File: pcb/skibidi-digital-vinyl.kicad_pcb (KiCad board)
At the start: 2 copper layers, 100 x 100 mm, 6 parts, among them U1 CH32V003FxUx, U2 BY25Q32ESHIG(R)

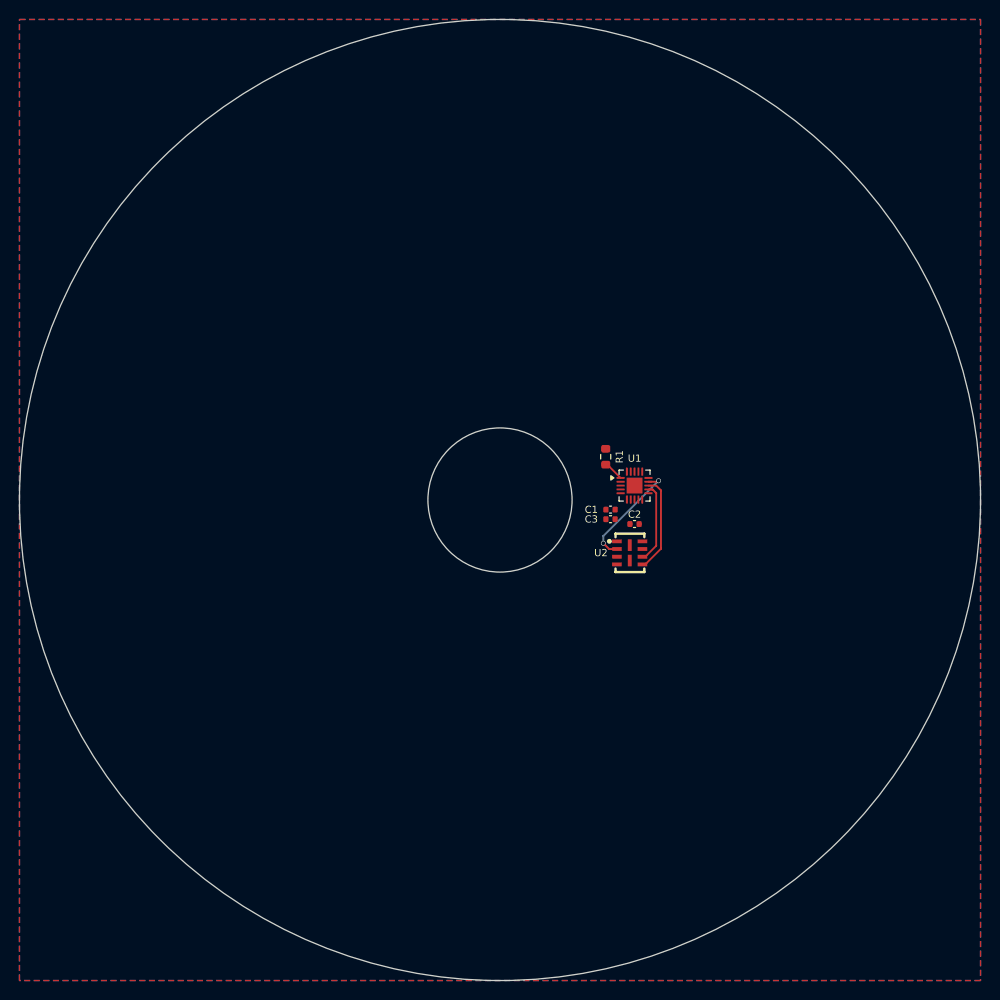
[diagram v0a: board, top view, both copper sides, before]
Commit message: disc routing done
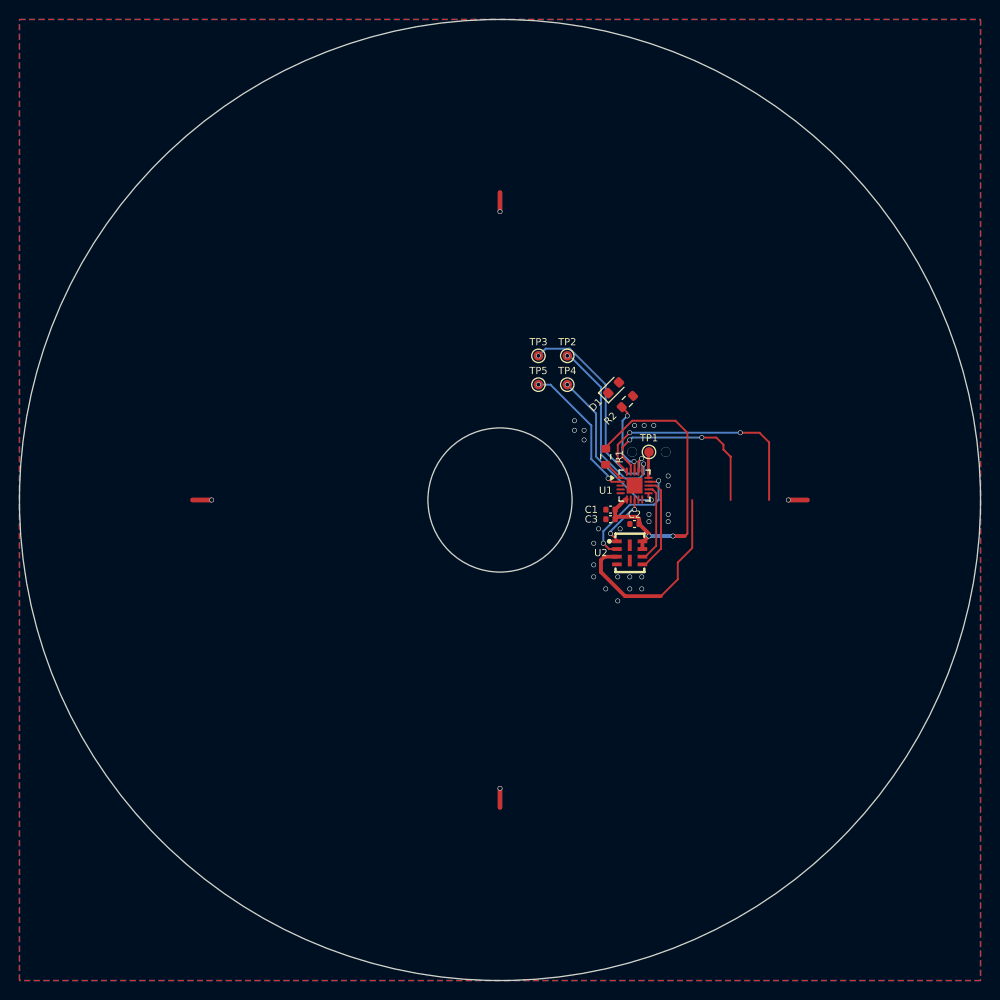
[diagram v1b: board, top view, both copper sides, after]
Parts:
- added D1: LED, LED_SMD:LED_0603_1608Metric, F.Cu at (161.8, 88.3)
- added R2: 1k, Resistor_SMD:R_0603_1608Metric, F.Cu at (163.2, 89.8)
- added TP1: TestPoint, TestPoint:TestPoint_Pad_D1.0mm, F.Cu at (165.5, 95.0)
- added TP2: TestPoint, TestPoint:TestPoint_Pad_D1.0mm, F.Cu at (157.0, 85.0)
- added TP3: TestPoint, TestPoint:TestPoint_Pad_D1.0mm, F.Cu at (154.0, 85.0)
- added TP4: TestPoint, TestPoint:TestPoint_Pad_D1.0mm, F.Cu at (157.0, 88.0)
- added TP5: TestPoint, TestPoint:TestPoint_Pad_D1.0mm, F.Cu at (154.0, 88.0)
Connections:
- R1 pad 1: +3V3 -> /RESET
- R1 pad 2: /RESET -> +3V3
- U1 pad 11: unconnected-(U1-PC4-Pad11) -> Net-(U1-PC4)
- U1 pad 16: unconnected-(U1-PD2-Pad16) -> Net-(U1-PD2)
- U1 pad 17: unconnected-(U1-PD3-Pad17) -> Net-(U1-PD3)
- U1 pad 2: unconnected-(U1-PA1-Pad2) -> Net-(U1-PA1)
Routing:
- net +3V3: track 0.00 -> 55.9 mm, vias 0 -> 2
- net /UART_RX: track 0.00 -> 25.9 mm, vias 0 -> 2
- net Net-(U1-PD3): track 0.00 -> 23.3 mm, vias 0 -> 2
- net /UART_TX: track 0.00 -> 20.2 mm, vias 0 -> 2
- net Net-(U1-PD2): track 0.00 -> 19.4 mm, vias 0 -> 2
- net Net-(U1-PC4): track 0.00 -> 17.2 mm, vias 0 -> 2
- net Net-(U1-PA1): track 0.00 -> 14.9 mm, vias 0 -> 2
- net GND: track 0.00 -> 8.00 mm, vias 0 -> 29
- net /LED: track 0.00 -> 7.95 mm, vias 0 -> 2
- net /CS: track 0.00 -> 5.81 mm, vias 0 -> 2
- net /SWIO: track 0.00 -> 2.72 mm
- net /MISO: track 11.6 -> 13.1 mm
- net (no net): vias 0 -> 2

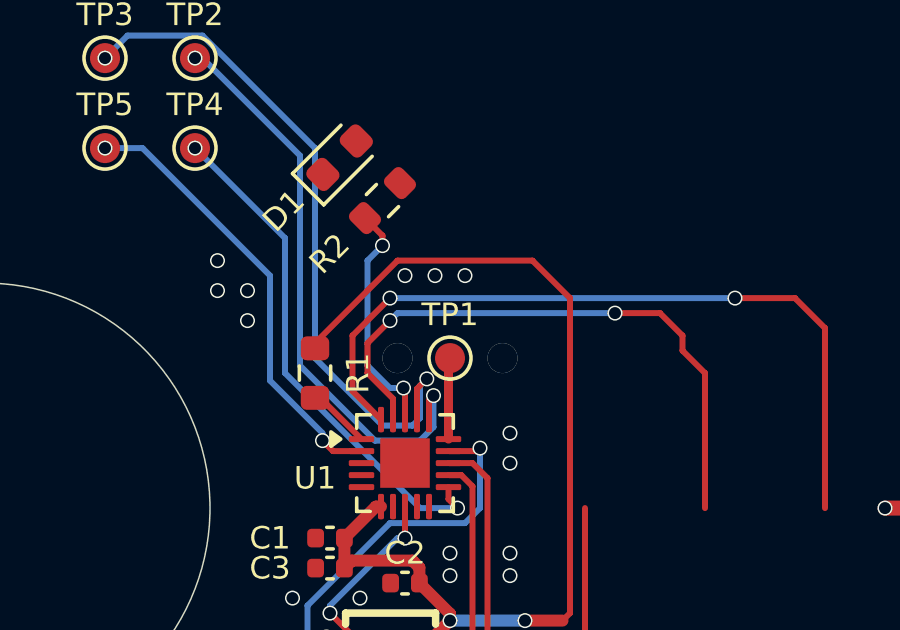
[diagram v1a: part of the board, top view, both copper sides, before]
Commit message: update silkscreen text
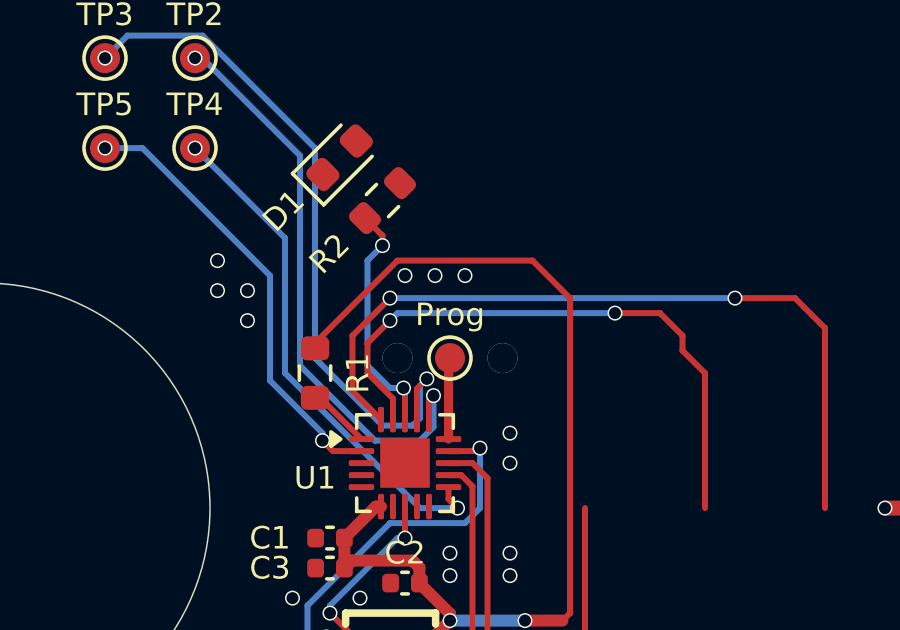
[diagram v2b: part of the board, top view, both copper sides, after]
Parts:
- renumbered TP1 to Prog
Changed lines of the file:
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@@
 		(descr "SMD pad as test Point, diameter 1.0mm")
 		(tags "test point SMD pad")
-		(property "Reference" "TP1"
+		(property "Reference" "Prog"
 			(at 0 -1.448 0)
 			(layer "F.SilkS")
